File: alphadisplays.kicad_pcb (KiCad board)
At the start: 2 copper layers, 8 parts

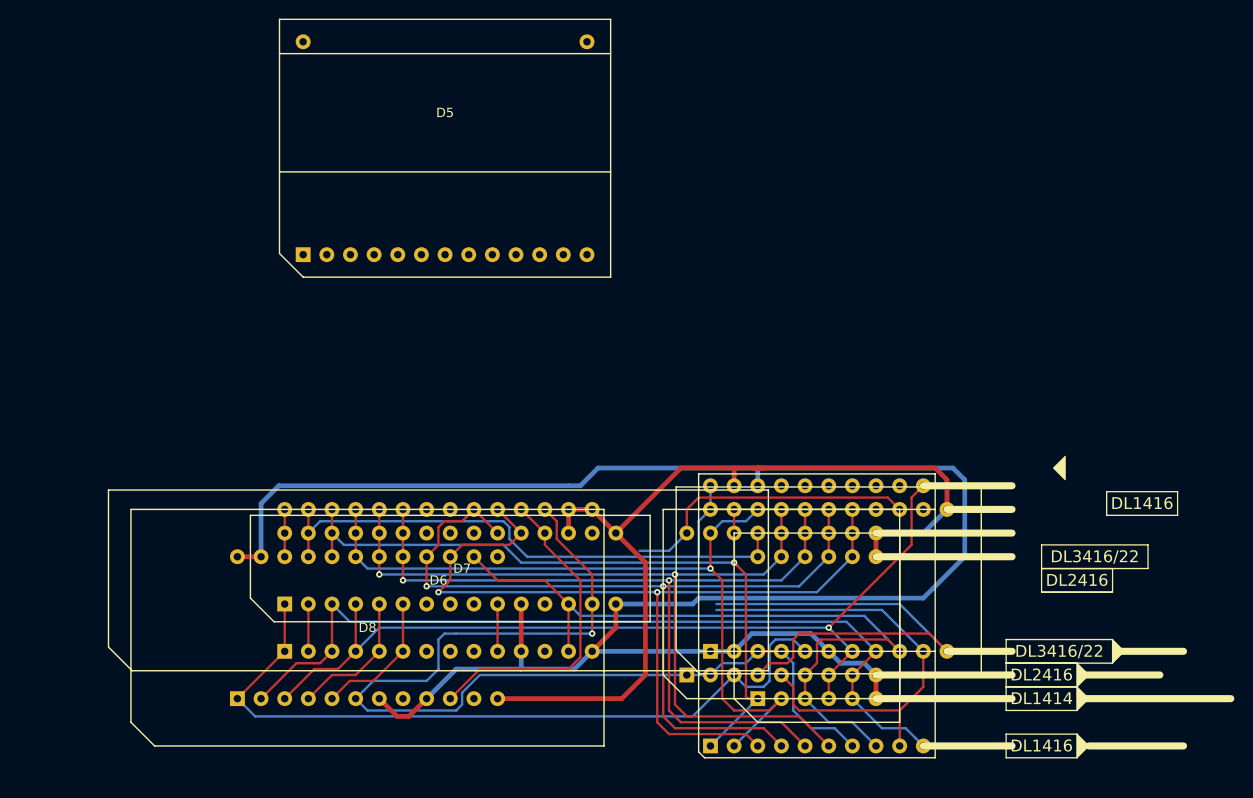
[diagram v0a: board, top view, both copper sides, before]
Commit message: tester board ready for fab
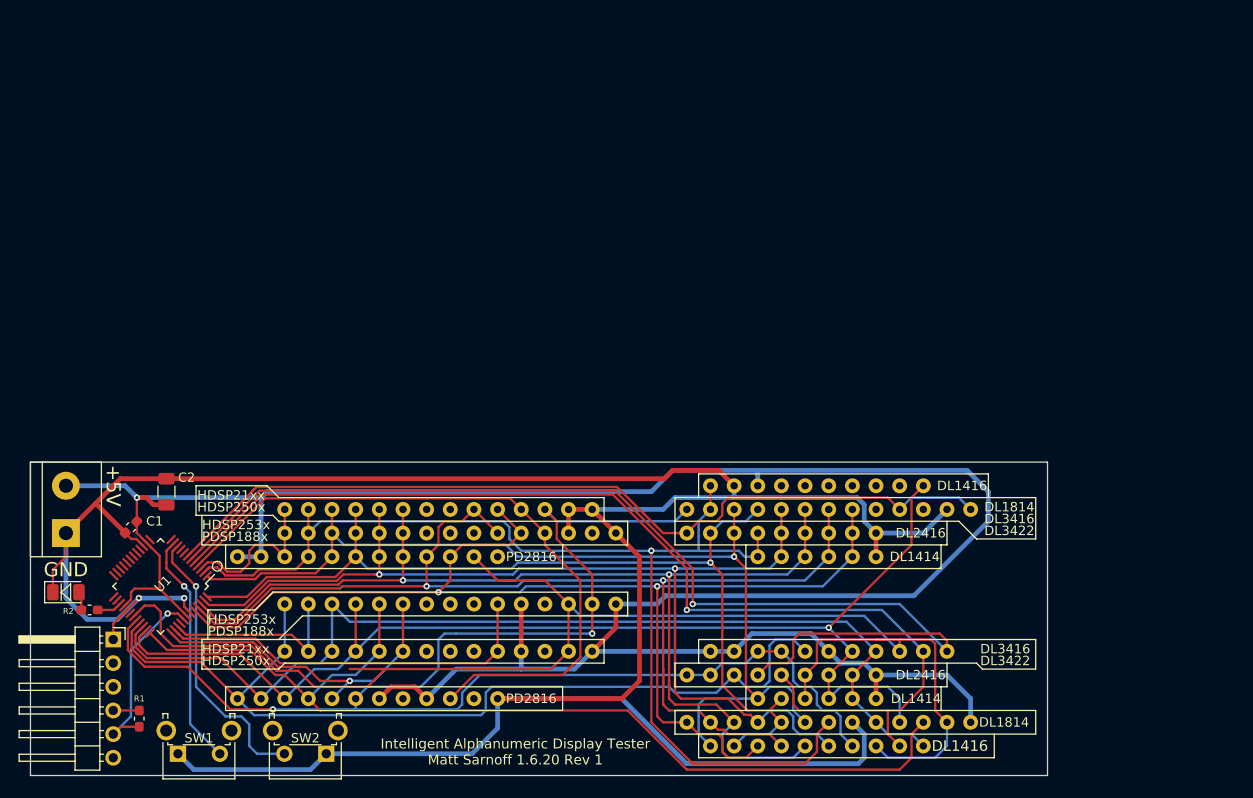
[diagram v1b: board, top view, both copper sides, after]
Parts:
- added C1: 0.1uF, Capacitor_SMD:C_0603_1608Metric_Pad1.05x0.95mm_HandSolder, F.Cu at (171.4, 45.1)
- added C2: 10uF, Capacitor_SMD:C_1206_3216Metric, F.Cu at (175.3, 41.3)
- added D9: LED, LED_SMD:LED_1206_3216Metric, F.Cu at (164.5, 52.1)
- added J1: FTDI 5V, Connector_PinHeader_2.54mm:PinHeader_1x06_P2.54mm_Horizontal, F.Cu at (169.5, 57.1)
- added J2: Screw_Terminal_01x02, TerminalBlock:TerminalBlock_bornier-2_P5.08mm, F.Cu at (164.5, 40.6)
- added R1: 4.7k, Resistor_SMD:R_0603_1608Metric_Pad1.05x0.95mm_HandSolder, F.Cu at (172.3, 65.6)
- added R2: 1k, Resistor_SMD:R_0603_1608Metric_Pad1.05x0.95mm_HandSolder, F.Cu at (167.0, 54.0)
- added SW1: SW_SPST, Button_Switch_THT:SW_Tactile_SPST_Angled_PTS645Vx31-2LFS, F.Cu at (181.0, 69.4)
- added SW2: SW_SPST, Button_Switch_THT:SW_Tactile_SPST_Angled_PTS645Vx31-2LFS, F.Cu at (192.4, 69.4)
- added U1: ATmega4809-A, Package_QFP:TQFP-48_7x7mm_P0.5mm, F.Cu at (174.6, 51.4)
- moved D5 65.0 mm to (231.1, 66.0)
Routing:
- net GND: track 98.7 -> 294.7 mm, vias 0 -> 2
- net /A2: track 14.8 -> 107.5 mm
- net /~WR: track 80.7 -> 154.8 mm
- net /CUE: track 50.9 -> 118.4 mm, vias 0 -> 1
- net /~CU: track 50.7 -> 118.0 mm, vias 0 -> 1
- net /~BL: track 32.3 -> 93.3 mm
- net VCC: track 211.0 -> 271.3 mm, vias 0 -> 1
- net /D6: track 66.9 -> 121.4 mm, vias 0 -> 1
- net /~CE: track 110.0 -> 157.7 mm, vias 1 -> 2
- net /~RD: track 34.3 -> 72.6 mm
- net /A4: track 5.08 -> 41.8 mm
- net /A1: track 95.8 -> 127.0 mm
- net /D0: track 93.5 -> 124.3 mm
- net /~SW2: track 0.00 -> 30.2 mm, vias 0 -> 1
- net /D2: track 87.1 -> 116.5 mm
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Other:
- board outline added: 109.2 x 33.7 mm
- board text added: "+5V"
- board text added: "DL1814"
- board text added: "DL3416"
- board text added: "DL3422"
- board text added: "GND"
- board text added: "HDSP21xx"
- board text added: "HDSP250x"
- board text added: "HDSP253x"
- board text added: "Intelligent Alphanumeric Display Tester Matt Sarnoff 1.6.20 Rev 1"
- board text added: "PD2816"
- board text added: "PDSP188x"
- board text removed: "DL3416/22"

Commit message: swap A0/A1 on 3416/3422
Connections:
- D4 pad 7: /A1 -> /A0
- D4 pad 8: /A0 -> /A1
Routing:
- net /A1: track 127.0 -> 132.9 mm
- net /A0: track 109.5 -> 105.9 mm
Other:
- board text added: "5V FTDI cable for UPDI programming"
- board text added: "This is ground!"
- board text added: "This is the back! No components on this side!"

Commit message: update board rev number
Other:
- board text added: "Intelligent Alphanumeric Display Tester Matt Sarnoff 1.11.20 Rev 1.1"
- board text removed: "Intelligent Alphanumeric Display Tester Matt Sarnoff 1.6.20 Rev 1"
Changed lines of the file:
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@@
     (effects (font (size 1.524 1.524) (thickness 0.15)) (justify mirror))
   )
-  (gr_text "Intelligent Alphanumeric Display Tester\nMatt Sarnoff 1.6.20 Rev 1" (at 212.725 69.215) (layer F.SilkS)
+  (gr_text "Intelligent Alphanumeric Display Tester\nMatt Sarnoff 1.11.20 Rev 1.1" (at 212.725 69.215) (layer F.SilkS)
     (effects (font (size 1.0668 1.0668) (thickness 0.15)))
   )

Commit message: more board tweaks
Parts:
- added D10: D, Diode_SMD:D_SOD-323, F.Cu at (172.1, 43.8)
- moved C1 1.99 mm to (170.1, 43.7), turned to 270 degrees
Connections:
- D2 pad 9: /~CU -> /A3
- D3 pad 5: /~CU -> /A3
- D4 pad 10: /~CU -> /A3
- D6 pad 12: Net-(D6-Pad12) -> /HDSPCLK
- D7 pad 12: Net-(D7-Pad12) -> /HDSPCLK
- D8 pad 8: Net-(D8-Pad8) -> /PD2816CLK
- U1 pad 12: Net-(U1-Pad12) -> /HDSPCLK
- U1 pad 13: Net-(U1-Pad13) -> /PD2816CLK
- U1 pad 14: VCC -> Net-(D10-Pad1)
- U1 pad 28: VCC -> Net-(D10-Pad1)
- U1 pad 42: VCC -> Net-(D10-Pad1)
- U1 pad 5: /~CU -> Net-(U1-Pad5)
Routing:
- net /~CU: track 118.0 -> 0.00 mm, vias 1 -> 0
- net /A3: track 36.2 -> 125.5 mm
- net /HDSPCLK: track 0.00 -> 51.9 mm, vias 0 -> 1
- net /PD2816CLK: track 0.00 -> 37.7 mm, vias 0 -> 2
- net VCC: track 271.3 -> 253.8 mm
- net Net-(D10-Pad1): track 0.00 -> 17.2 mm
- net /D6: track 121.4 -> 123.7 mm
- net /~WR: track 155.2 -> 156.5 mm
- net /A4: track 41.8 -> 42.6 mm
- net /~CE: track 157.7 -> 156.9 mm
- net GND: track 294.7 -> 293.9 mm
- net /A1: track 132.9 -> 133.5 mm
- net /~RD: track 72.6 -> 73.1 mm
- net /~FL: track 20.2 -> 20.7 mm
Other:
- board text added: "Intelligent Alphanumeric Display Tester Matt Sarnoff 1.21.20 Rev 1.1"
- board text removed: "Intelligent Alphanumeric Display Tester Matt Sarnoff 1.11.20 Rev 1.1"

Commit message: board tweaks, docs
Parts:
- removed D10: D, Diode_SMD:D_SOD-323
- D6: footprint Display_IntelligentAlpha:HDSP-250x_DIP28 -> Display_IntelligentAlpha:HDSP-250x
- D7: footprint Display_IntelligentAlpha:PDSP188x_DIP30 -> Display_IntelligentAlpha:PDSP188x
- D9: value LED -> 1206 LED
- SW1, SW2: footprint Button_Switch_THT:SW_Tactile_SPST_Angled_PTS645Vx31-2LFS -> Button_Switch_SMD:Panasonic_EVQPUL_EVQPUC
- moved SW2 3.20 mm to (189.2, 69.3)
- moved SW1 1.93 mm to (179.1, 69.3)
- moved C1 1.09 mm to (170.8, 44.5), turned to 225 degrees
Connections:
- SW1 pad 1: /~SW1 -> GND
- SW1 pad 2: GND -> /~SW1
- U1 pad 14: Net-(D10-Pad1) -> VCC
- U1 pad 28: Net-(D10-Pad1) -> VCC
- U1 pad 42: Net-(D10-Pad1) -> VCC
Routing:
- net VCC: track 253.8 -> 271.6 mm
- net Net-(D10-Pad1): track 17.2 -> 0.00 mm
- net /~SW2: track 30.2 -> 34.8 mm, vias 1 -> 2
- net /~SW1: track 25.4 -> 29.2 mm, vias 1 -> 2
- net /D1: track 121.5 -> 120.3 mm
- net GND: track 293.9 -> 293.1 mm, vias 2 -> 3
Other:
- board text added: "Intelligent Alphanumeric Display Tester Matt Sarnoff 2.6.20 Rev 1.1"
- board text removed: "Intelligent Alphanumeric Display Tester Matt Sarnoff 1.21.20 Rev 1.1"

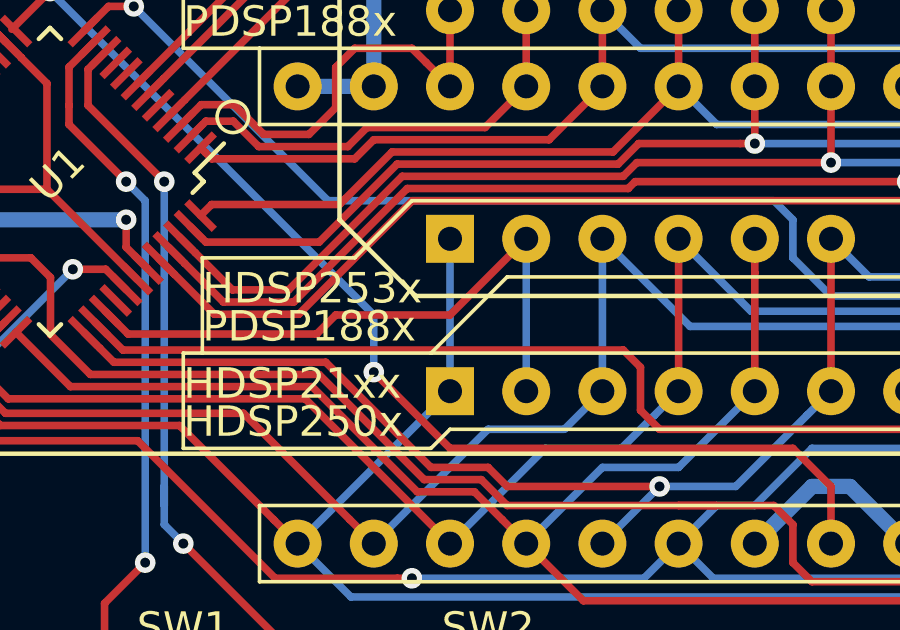
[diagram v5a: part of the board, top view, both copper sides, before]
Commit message: fix drc errors
(except overlapping courtyards, which are fine)
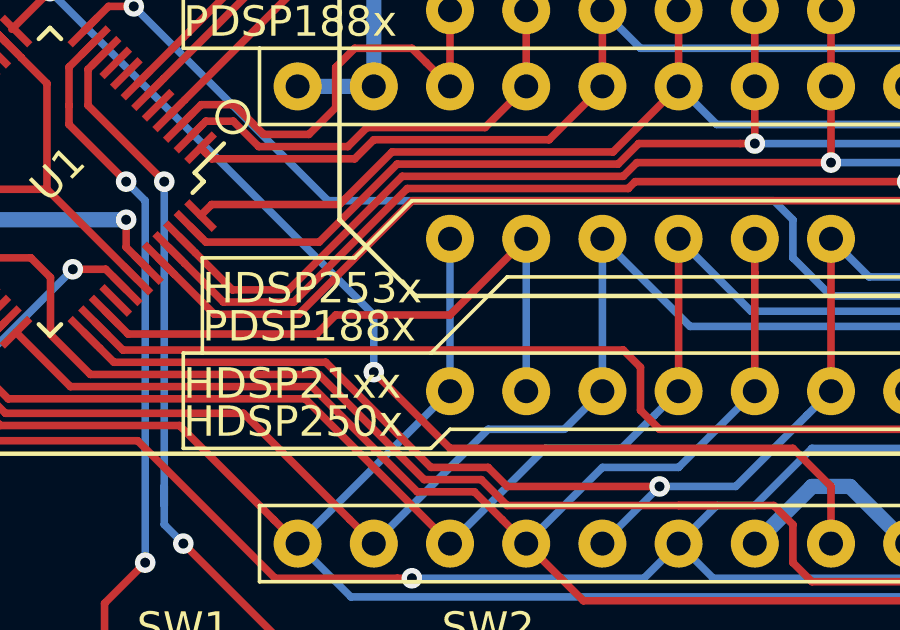
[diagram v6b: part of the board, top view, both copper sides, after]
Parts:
- U1: value ATmega4809-A -> ATmega809-A
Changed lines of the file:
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@@
     (mod_text_size 1 1)
     (mod_text_width 0.15)
-    (pad_size 1.75 1.75)
-    (pad_drill 0.99)
+    (pad_size 1.6 1.6)
+    (pad_drill 0.8)
     (pad_to_mask_clearance 0.051)
     (solder_mask_min_width 0.25)
@@
     (fp_line (start -3.683 -0.635) (end -1.143 1.905) (layer F.SilkS) (width 0.15))
     (fp_line (start -3.683 -9.525) (end -3.683 1.905) (layer F.CrtYd) (width 0.0508))
-    (fp_line (start -3.683 1.905) (end 39.243 1.905) (layer F.Fab) (width 0.0508))
+    (fp_line (start -3.683 1.905) (end 39.243 1.905) (layer F.CrtYd) (width 0.0508))
     (fp_line (start 39.243 -9.525) (end 39.243 1.905) (layer F.CrtYd) (width 0.0508))
     (fp_line (start -3.683 -9.525) (end 39.243 -9.525) (layer F.CrtYd) (width 0.0508))
@@
     (pad 17 thru_hole oval (at 33.02 -7.62 90) (size 1.6 1.6) (drill 0.8) (layers *.Cu *.Mask)
       (net 29 "Net-(D7-Pad17)"))
-    (pad 1 thru_hole rect (at 0 0 90) (size 1.6 1.6) (drill 0.8) (layers *.Cu *.Mask)
+    (pad 1 thru_hole circle (at 0 0 90) (size 1.6 1.6) (drill 0.8) (layers *.Cu *.Mask)
       (net 21 /~CLR))
   )
@@
     (pad 15 thru_hole oval (at 33.02 -15.24 90) (size 1.6 1.6) (drill 0.8) (layers *.Cu *.Mask)
       (net 1 GND))
-    (pad 1 thru_hole rect (at 0 0 90) (size 1.6 1.6) (drill 0.8) (layers *.Cu *.Mask)
+    (pad 1 thru_hole oval (at 0 0 90) (size 1.6 1.6) (drill 0.8) (layers *.Cu *.Mask)
       (net 21 /~CLR))
   )
@@
       (effects (font (size 1 1) (thickness 0.15)))
     )
-    (fp_text value ATmega4809-A (at 0 6 45) (layer F.Fab)
+    (fp_text value ATmega809-A (at 0 6 45) (layer F.Fab)
       (effects (font (size 1 1) (thickness 0.15)))
     )
@@
   (segment (start 185.42 55.879982) (end 185.42 57.785) (width 0.254) (layer B.Cu) (net 62))
   (segment (start 174.625 45.084982) (end 185.42 55.879982) (width 0.254) (layer B.Cu) (net 62))
-  (segment (start 199.39 60.325) (end 187.96 60.325) (width 0.254) (layer F.Cu) (net 62))
+  (segment (start 200.66 63.5) (end 200.66 61.595) (width 0.254) (layer F.Cu) (net 62))
   (segment (start 187.96 60.325) (end 185.42 57.785) (width 0.254) (layer F.Cu) (net 62))
   (segment (start 200.66 61.595) (end 199.39 60.325) (width 0.254) (layer F.Cu) (net 62))
-  (segment (start 200.66 63.5) (end 200.66 61.595) (width 0.254) (layer F.Cu) (net 62))
+  (segment (start 199.39 60.325) (end 187.96 60.325) (width 0.254) (layer F.Cu) (net 62))
 )
